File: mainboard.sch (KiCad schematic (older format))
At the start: 72 parts, among them IC1 ATXMEGA128A1U-A, J1 USB, K1 X_MIN, K2 X_MAX, K3 Y_MIN, K4 Y_MAX, K5 Z_MIN, K6 Z_MAX, P1 POWER, P10 USART, P11 TH_HB, P12 TH_EX, P13 TH_HO, P14 LCD, P2 PDI, P3 GPIO_B, P4 BEEPER, P5 OPEN_C_OUT, P6 12V, P7 5V, P8 3.3V, P9 I2C, U1 NE 4558 D SMD, U2 ULN_2003_A

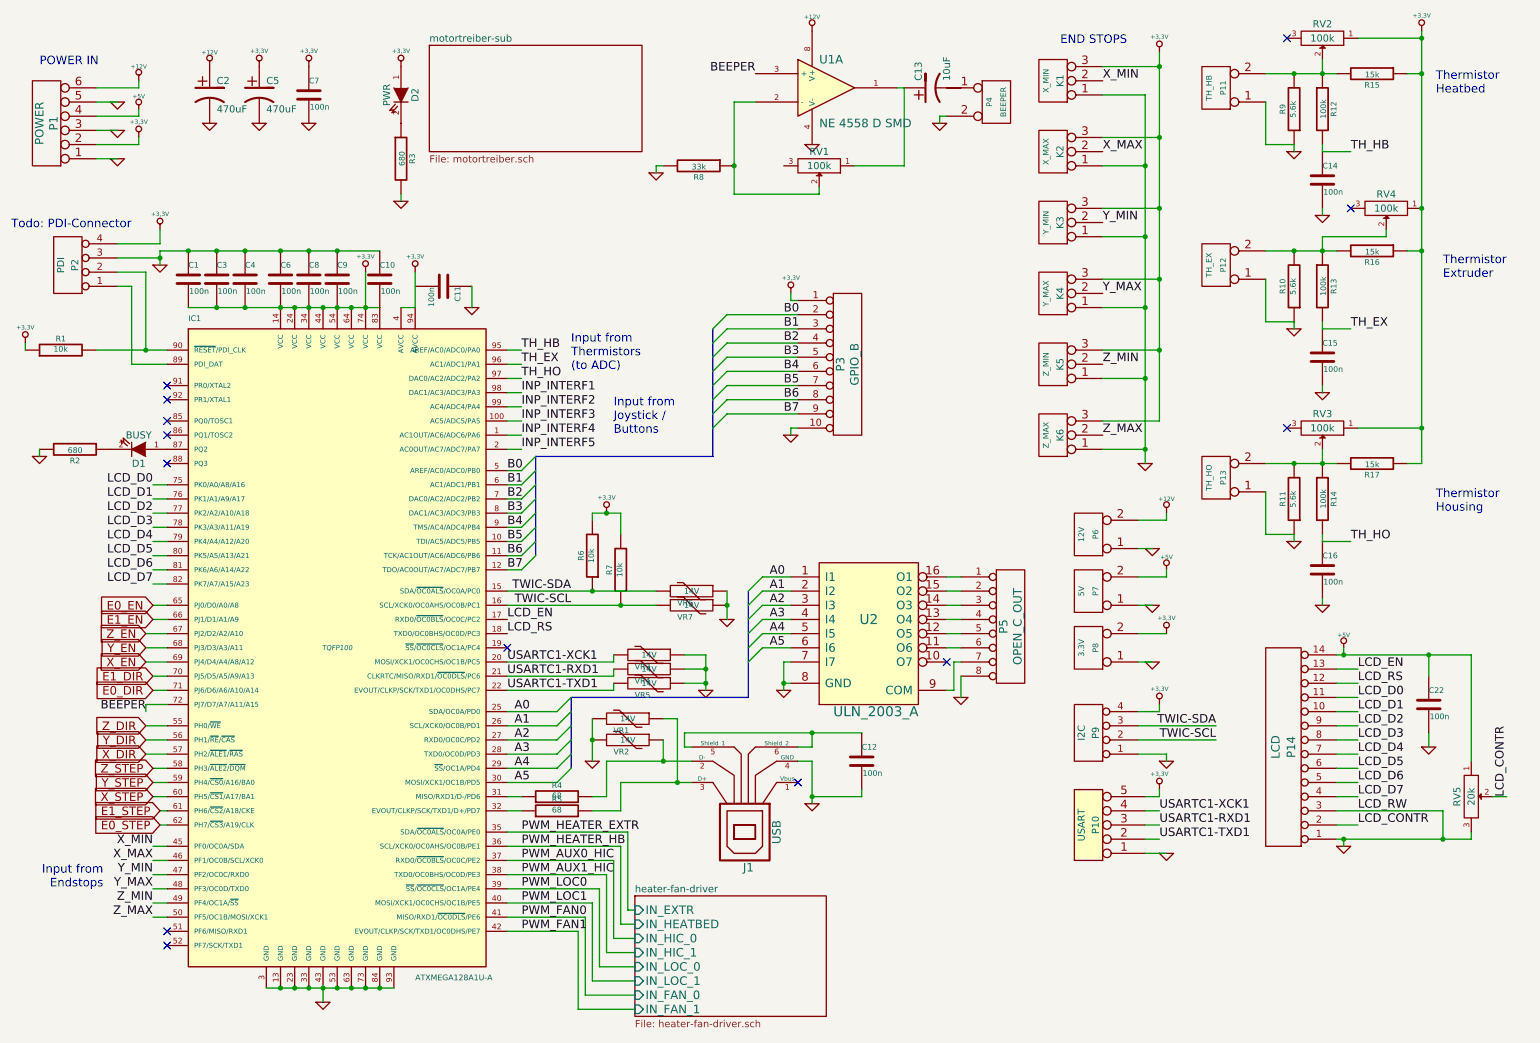
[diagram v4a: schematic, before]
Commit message: Added status LEDs for 5V and 12V power
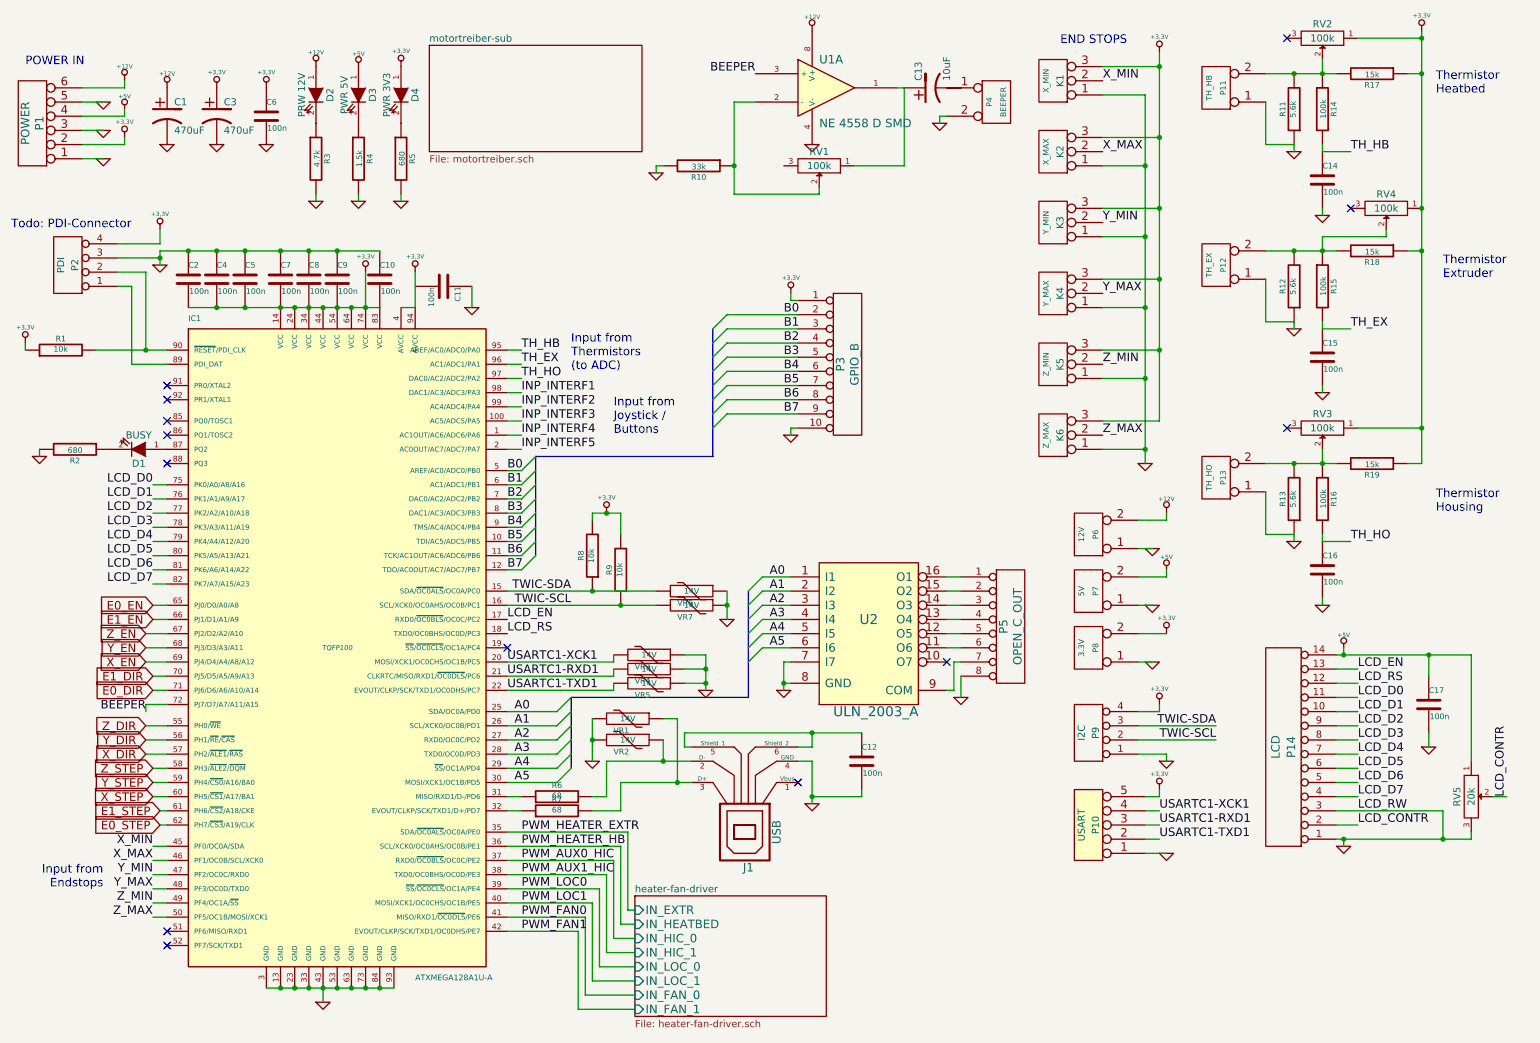
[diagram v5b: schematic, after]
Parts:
- added D2: PRW 12V, symbol LED
- added D3: PWR 5V, symbol LED
- added R3: 4.7k, symbol R
- added R4: 1.5k, symbol R
- D4: renamed from D2; value PWR -> PWR 3V3; Color (none) -> Red
- renumbered C2 to C1, C22 to C17, C1 to C2, C5 to C3, C3 to C4, C4 to C5, C7 to C6, C6 to C7, R8 to R10, R9 to R11, R10 to R12, R11 to R13, R12 to R14, R13 to R15, R14 to R16, R15 to R17, R16 to R18, R17 to R19, R3 to R5, R4 to R6, R5 to R7, R6 to R8, R7 to R9
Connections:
- net +12V: now also D2.1 (A)
- net +5V: now also D3.1 (A)
- net GND: now also R3.2, R4.2
- new net: D3.2 (K), R4.1
- new net: D2.2 (K), R3.1
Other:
- moved on the sheet: C1, C3, C6, P1

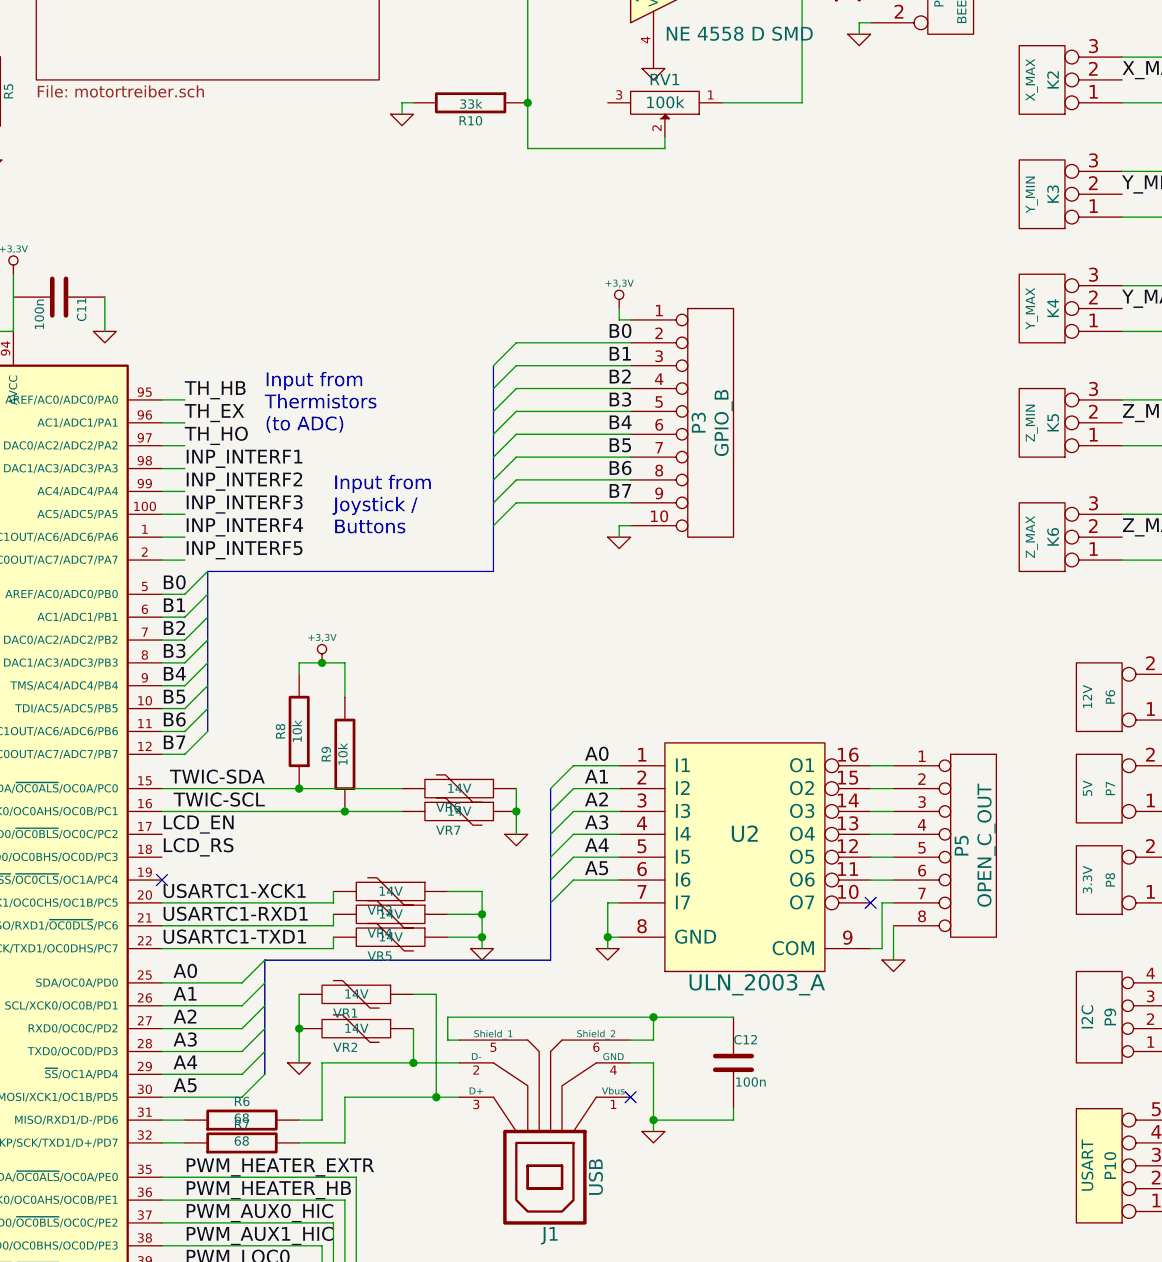
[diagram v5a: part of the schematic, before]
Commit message: Added missing interface connector; reworked schematic. Started to layout PCB
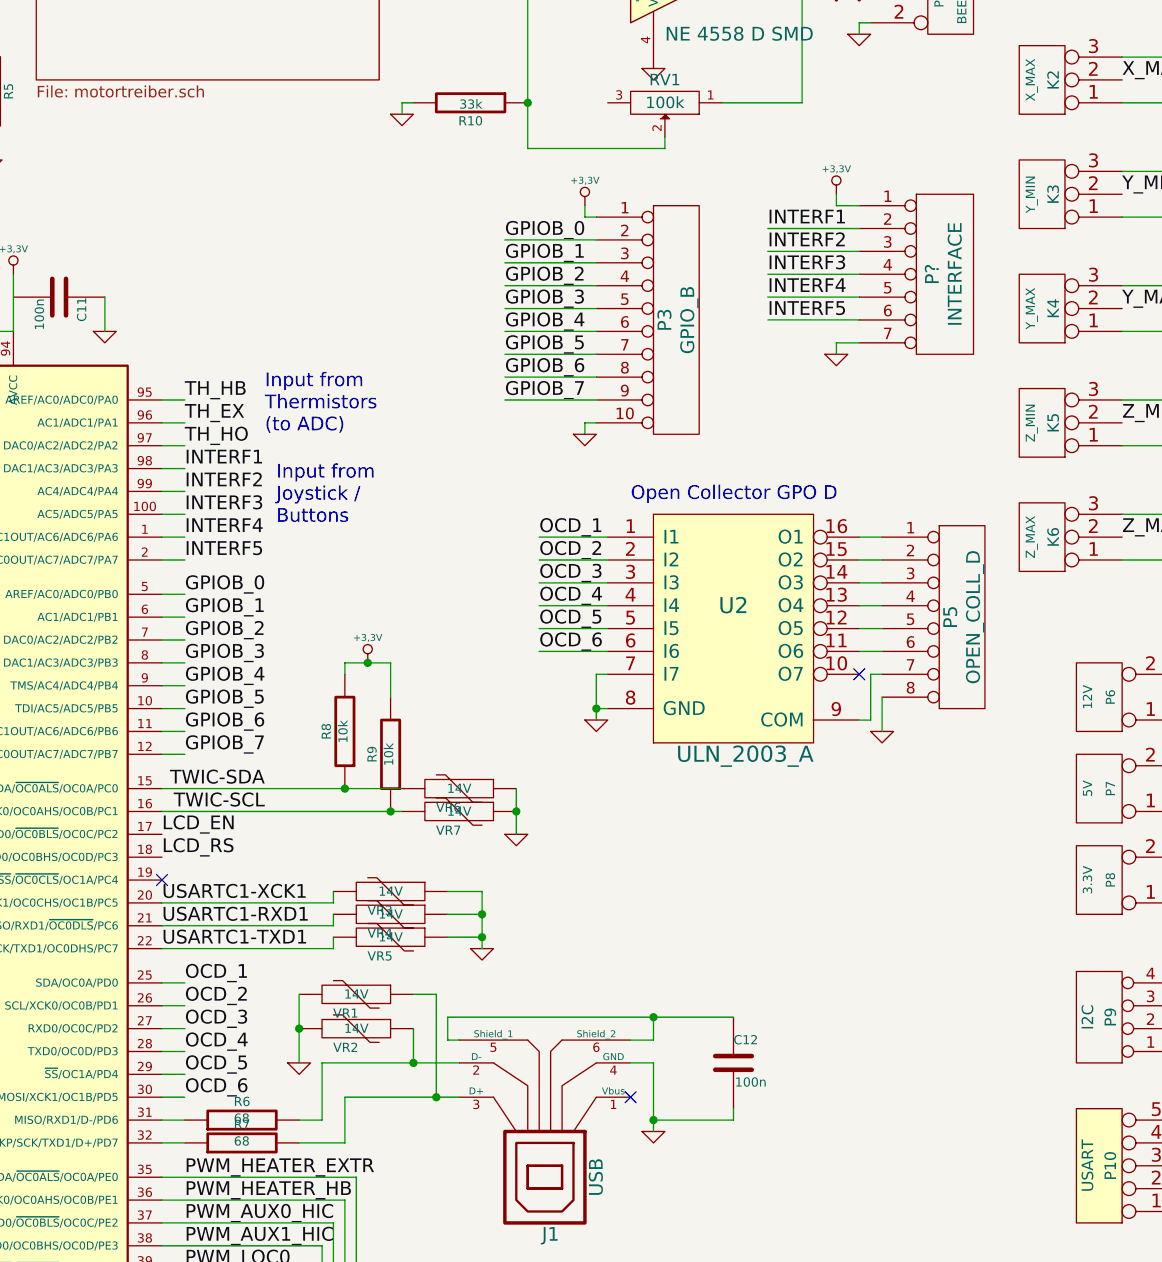
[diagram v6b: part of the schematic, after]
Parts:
- added P?: INTERFACE, symbol CONN_7
- P5: value OPEN_C_OUT -> OPEN_COLL_D
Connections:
- net +3.3V: now also P?.1 (P1)
- net GND: now also P?.7 (P7)
- net A0 renamed OCD_1
- net A1 renamed OCD_2
- net A2 renamed OCD_3
- net A3 renamed OCD_4
- net A4 renamed OCD_5
- net A5 renamed OCD_6
- net B0 renamed GPIOB_0
- net B1 renamed GPIOB_1
- net B2 renamed GPIOB_2
- net B3 renamed GPIOB_3
- net B4 renamed GPIOB_4
- net B5 renamed GPIOB_5
- net B6 renamed GPIOB_6
- net B7 renamed GPIOB_7
- net INP_INTERF1 renamed INTERF1
- net INTERF1: now also P?.2 (P2)
- net INP_INTERF2 renamed INTERF2
- net INTERF2: now also P?.3 (P3)
- net INP_INTERF3 renamed INTERF3
- net INTERF3: now also P?.4 (P4)
- net INP_INTERF4 renamed INTERF4
- net INTERF4: now also P?.5 (P5)
- net INP_INTERF5 renamed INTERF5
- net INTERF5: now also P?.6 (P6)
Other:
- note added: "Open Collector GPO D"
- moved on the sheet: P3, P5, R8, R9, U2

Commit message: Reworked schematic
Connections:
- net USB-: now reaches J1.2 (D-), R6.2, VR2.1
- net USB+: now reaches J1.3 (D+), R7.2, VR1.1
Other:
- moved on the sheet: C12, J1, P6, P7, P8, VR1, VR2

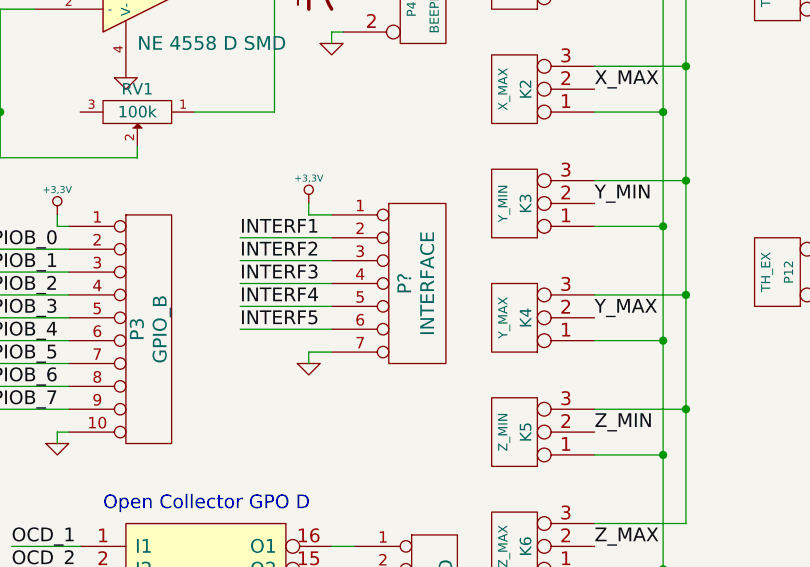
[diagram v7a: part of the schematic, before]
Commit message: * Changed connectors to PSK type - this prevents plugging the steppers in the wrong way * Changed stepping increment jumpers to DIP-switches - easier setting
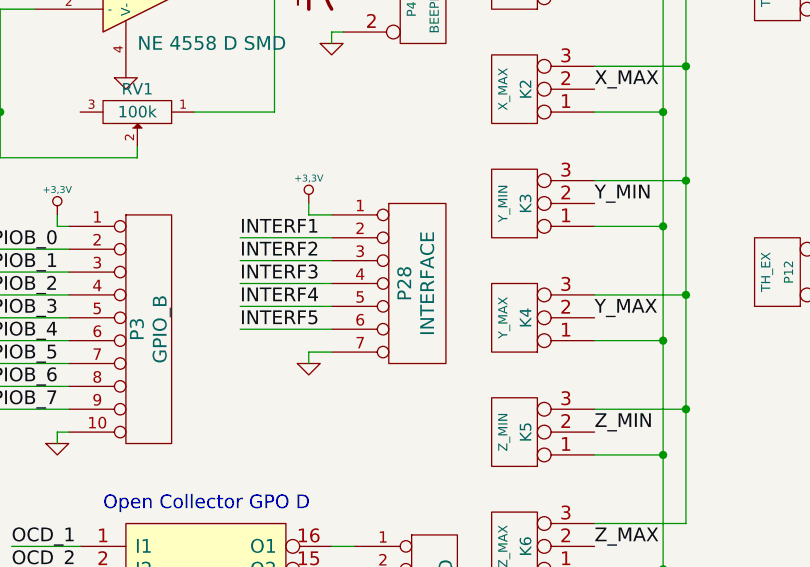
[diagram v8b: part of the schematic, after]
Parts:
- gave numbers to parts that had none: 1
